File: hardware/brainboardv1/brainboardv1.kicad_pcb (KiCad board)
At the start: 4 copper layers, 86.4 x 54.6 mm, 86 parts, among them P1 WP, P2 CONN_12, P3 CONN_5X2, P4 BTRST, P5 GND, P6 5VD, P7 3V3, P8 5VA, U1 24C256, U10 TPS73150, U2 BEAGLEBONE_BLACK, U3 OPA2376, U4 ADS1299, U5 TPD4E001, U6 TPD4E001, U7 TPD4E001, U8 ATUC3L064, U9 BLUETOOTH-RN42

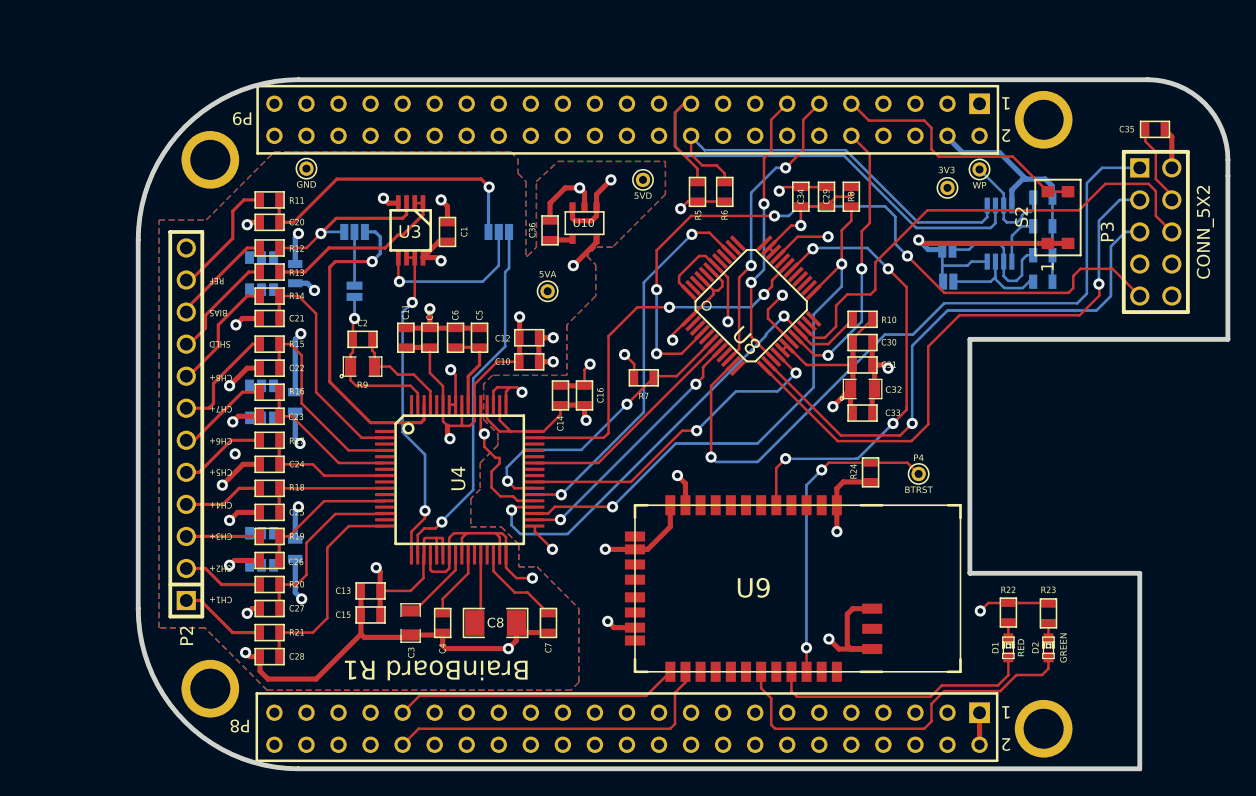
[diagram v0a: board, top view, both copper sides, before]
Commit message: Nearly finished v1 sch & brd, await final check
Fixed errors from Rev 0, added MPU-6050 accelerometer/gyro for head
motion tracking, switched to +/-2.5V analog supply, added 2 bipolar
analog inputs for EOG tracking, added daisy-chain capability
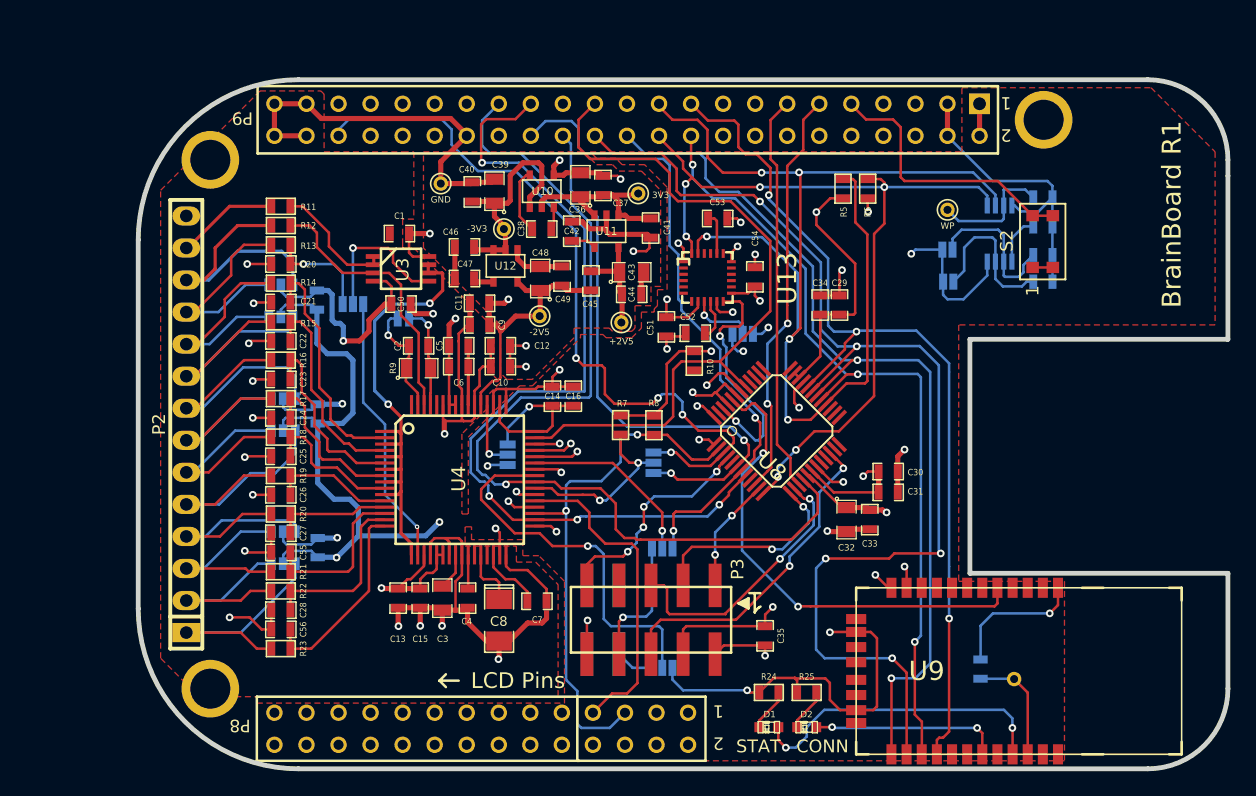
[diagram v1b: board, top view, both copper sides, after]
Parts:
- added C37: 1uF, SM0603_Capa, F.Cu at (189.2, 122.0)
- added C38: 1uF, SM0603_Capa, F.Cu at (184.4, 125.5)
- added C39: 10uF, SM0805, F.Cu at (180.6, 122.5)
- added C40: 1uF, SM0603_Capa, F.Cu at (178.9, 122.6)
- added C41: 1uF, SM0603_Capa, F.Cu at (193.0, 125.4)
- added C42: 0.01uF, SM0603_Capa, F.Cu at (186.8, 125.7)
- added C43: 10uF, SM0805, F.Cu at (191.5, 128.9)
- added C44: 2.2uF, SM0603_Capa, F.Cu at (191.5, 130.7)
- added C45: 0.1uF, SM0603_Capa, F.Cu at (188.3, 129.6)
- added C46: 1uF, SM0603_Capa, F.Cu at (178.3, 126.9)
- added C47: 0.01uF, SM0603_Capa, F.Cu at (178.3, 129.4)
- added C48: 10uF, SM0805, F.Cu at (184.3, 129.4)
- added C49: 2.2uF, SM0603_Capa, F.Cu at (186.0, 129.2)
- added C50: 0.1uF, SM0603_Capa, F.Cu at (173.2, 131.4)
- added C51: 0.1uF, SM0603_Capa, F.Cu at (194.3, 133.2)
- added C52: 0.1uF, SM0603_Capa, F.Cu at (196.5, 133.8)
- added C53: 2.2nF, SM0603_Capa, F.Cu at (198.3, 124.7)
- added C54: 0.01uF, SM0603_Capa, F.Cu at (201.3, 129.3)
- added C55: 4.7nF, SM0603_Capa, F.Cu at (163.7, 151.1)
- added C56: 4.7nF, SM0603_Capa, F.Cu at (163.7, 157.2)
- added P10: CONN_2X2, bb02-hp04, B.Cu at (189.2, 156.5)
- added P9: -2V5, PINTST, F.Cu at (184.2, 132.4)
- added R25: 330, SM0603, F.Cu at (205.4, 162.2)
- added R26: 10K, SM0603, B.Cu at (219.2, 160.4)
- added SJ6: DAISY_OUT, SparkFun-Passives-SJ_3_PASTE2&3, B.Cu at (193.9, 150.8)
- added SJ7: DAISY_CS, SparkFun-Passives-SJ_3_PASTE2&3, B.Cu at (193.9, 160.3)
- added SJ8: CLKSEL, SparkFun-Passives-SJ_3_PASTE1&2, B.Cu at (181.7, 143.4)
- added SJ9: I2C Address Select (2&3NC), SparkFun-Passives-SJ_3_PASTE2&3, B.Cu at (200.3, 133.8)
- added U11: TPS73225, SOT23-5, F.Cu at (189.5, 125.7)
- added U12: TPS72325, SOT23-5, F.Cu at (181.5, 128.4)
- added U13: MPU6050, QFN24-4x4, F.Cu at (197.5, 129.3)
- C1, C10, C11, C12, C13, C14, C15, C16, C17, C18, C19, C2, C20, C21, C22, C23, C24, C25, C26, C27, C28, C29, C30, C31, C33, C34, C35, C4, C5, C6, C7, C9: footprint SM0603 -> SM0603_Capa
- C36: value 0.1uF -> 10uF; footprint SM0603 -> SM0805
- C8: footprint SM1206 -> SM1206POL
- D1: value RED -> STAT
- D2: value GREEN -> CONN
- P2: value CONN_12 -> CONN_14; footprint PIN_ARRAY-12X1 -> pin_strip_14
- P3: footprint PIN_ARRAY_5x2 -> bb02-hp10
- P4: moved to B.Cu
- P6: value 5VD -> -3V3
- P8: value 5VA -> +2V5
- R22, R23: value 330 -> 4.99K
- R24: value 10K -> 330
- SJ1: value SOLDERJUMPER_2WAYPASTE2&3 -> REF-SRB2
- SJ2: value SOLDERJUMPER_2WAYPASTE2&3 -> DAISY_CS
- SJ3: value SOLDERJUMPERNO -> NO BIAS FILT
- SJ4: value SOLDERJUMPERNC2 -> A2
- SJ5: value SOLDERJUMPERNC2 -> A1
- U10: value TPS73150 -> TPS60403
- U2: footprint BEAGLEBONE_BLACK -> BEAGLEBONE_BLACK_EEGMOD
- U5, U6, U7: value TPD4E001 -> TPD4E001DBV
- moved R23 60.9 mm to (163.7, 158.8), turned to 0 degrees
- moved R22 57.7 mm to (163.7, 154.2), turned to 0 degrees
- moved C35 50.6 mm to (202.1, 157.7), turned to 270 degrees
- moved P3 50.4 mm to (193.0, 156.5), turned to 180 degrees
- moved SJ2 29.9 mm to (193.2, 144.0), turned to 270 degrees
- moved P7 24.5 mm to (192.0, 122.7)
- moved R8 23.9 mm to (193.3, 141.0)
- moved D2 20.2 mm to (205.4, 165.0), turned to 180 degrees
- moved D1 20.0 mm to (202.4, 165.0), turned to 180 degrees
- moved R24 19.2 mm to (202.4, 162.2), turned to 180 degrees
- moved U9 18.7 mm to (218.7, 160.5)
- moved P4 17.9 mm to (221.8, 161.2)
- moved R10 13.7 mm to (196.5, 135.9), turned to 270 degrees
- moved SJ1 12.9 mm to (169.4, 131.4)
- moved P6 11.7 mm to (181.4, 125.5)
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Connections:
- C1 pad 1: +5VA -> +2.5V
- C10 pad 1: +5VA -> +2.5V
- C11 pad 1: +5VA -> +2.5V
- C11 pad 2: AGND -> -2.5V
- C12 pad 1: +5VA -> +2.5V
- C13 pad 1: +5VA -> +2.5V
- C13 pad 2: AGND -> -2.5V
- C14 pad 1: 3V3 -> +3.3V
- C15 pad 1: +5VA -> +2.5V
- C15 pad 2: AGND -> -2.5V
- C16 pad 1: 3V3 -> +3.3V
- C17 pad 1: +5VA -> +2.5V
- C17 pad 2: AGND -> -2.5V
- C18 pad 1: +5VA -> +2.5V
- C18 pad 2: AGND -> -2.5V
- C19 pad 1: +5VA -> +2.5V
- C19 pad 2: AGND -> -2.5V
- C27 pad 1: AIN2P -> AIN2N
- C28 pad 1: AIN1P -> AIN1N
- C29 pad 1: 3V3 -> +3.3V
- C3 pad 1: AGND -> -2.5V
- C30 pad 1: 3V3 -> +3.3V
- C31 pad 1: 3V3 -> +3.3V
- C32 pad 1: 3V3 -> +3.3V
- C33 pad 1: 3V3 -> +3.3V
- C34 pad 1: 3V3 -> +3.3V
- C35 pad 1: 3V3 -> +3.3V
- C36 pad 1: N-00000204 -> +3.3V
- C4 pad 2: AGND -> -2.5V
- C5 pad 2: AGND -> -2.5V
- C6 pad 2: AGND -> -2.5V
- C7 pad 2: AGND -> -2.5V
- C8 pad 2: AGND -> -2.5V
- C9 pad 1: +5VA -> +2.5V
- C9 pad 2: AGND -> -2.5V
- D1 pad 2: N-00000194 -> N-00000159
- D2 pad 2: N-00000193 -> N-00000157
- P2 pad 10: /BrainBoard Analog In/BIAS_ELEC -> /BrainBoard Analog In/CH8ELEC_P
- P2 pad 12: (no net) -> /BrainBoard Analog In/BIAS_ELEC
- P2 pad 2: /BrainBoard Analog In/CH2ELEC_P -> /BrainBoard Analog In/CH1ELEC_N
- P2 pad 3: /BrainBoard Analog In/CH3ELEC_P -> /BrainBoard Analog In/CH2ELEC_P
- P2 pad 4: /BrainBoard Analog In/CH4ELEC_P -> /BrainBoard Analog In/CH2ELEC_N
- P2 pad 5: /BrainBoard Analog In/CH5ELEC_P -> /BrainBoard Analog In/CH3ELEC_P
- P2 pad 6: /BrainBoard Analog In/CH6ELEC_P -> /BrainBoard Analog In/CH4ELEC_P
- P2 pad 7: /BrainBoard Analog In/CH7ELEC_P -> /BrainBoard Analog In/CH5ELEC_P
- P2 pad 8: /BrainBoard Analog In/CH8ELEC_P -> /BrainBoard Analog In/CH6ELEC_P
- P2 pad 9: /BrainBoard Analog In/BIAS_SHD -> /BrainBoard Analog In/CH7ELEC_P
- P3 pad 4: 3V3 -> +3.3V
- P3 pad 8: (no net) -> DAISY_OUT
- P6 pad 1: +5VD -> -3.3V
- P7 pad 1: 3V3 -> +3.3V
- P8 pad 1: +5VA -> +2.5V
- R1 pad 1: 3V3 -> +3.3V
- R10 pad 1: 3V3 -> +3.3V
- R10 pad 2: /RESET -> /BrainBoard AFE//RESET
- R11 pad 1: /BrainBoard Analog In/REF_ELEC -> /BrainBoard Analog In/BIAS_SHD
- R11 pad 2: REF -> SHIELD
- R13 pad 1: /BrainBoard Analog In/BIAS_SHD -> /BrainBoard Analog In/REF_ELEC
- R13 pad 2: SHIELD -> REF
- R2 pad 1: 3V3 -> +3.3V
- R20 pad 1: /BrainBoard Analog In/CH2ELEC_P -> /BrainBoard Analog In/CH2ELEC_N
- R20 pad 2: AIN2P -> AIN2N
- R21 pad 1: /BrainBoard Analog In/CH1ELEC_P -> /BrainBoard Analog In/CH2ELEC_P
- R21 pad 2: AIN1P -> AIN2P
- R22 pad 1: N-00000194 -> /BrainBoard Analog In/CH1ELEC_N
- R22 pad 2: AGND -> AIN1N
- R23 pad 1: N-00000193 -> /BrainBoard Analog In/CH1ELEC_P
- R23 pad 2: AGND -> AIN1P
- R24 pad 1: /BrainBoard Bluetooth/FACTORY -> N-00000159
- R3 pad 1: 3V3 -> +3.3V
- R4 pad 1: 3V3 -> +3.3V
- R5 pad 1: 3V3 -> +3.3V
- R5 pad 2: /SCL -> I2C2_SCL
- R6 pad 1: 3V3 -> +3.3V
- R6 pad 2: /SDA -> I2C2_SDA
- R7 pad 1: 3V3 -> +3.3V
- R7 pad 2: /CS -> /BrainBoard AFE//CS
- R8 pad 1: 3V3 -> +3.3V
- SJ2 pad 1: /BrainBoard AFE/BIASIN -> /CS_DAISY
- SJ2 pad 2: N-0000099 -> /BrainBoard AFE//CS
- SJ2 pad 3: BIAS -> /CS_MAIN
- SJ3 pad 1: N-0000099 -> /BrainBoard AFE/BIASINV
- U1 pad 5: /SDA -> I2C2_SDA
- U1 pad 6: /SCL -> I2C2_SCL
- U1 pad 8: 3V3 -> +3.3V
- U10 pad 1: +5VD -> -3.3V
- U10 pad 2: AGND -> +3.3V
- U10 pad 3: +5VD -> N-00000168
- U10 pad 4: N-00000204 -> AGND
- U10 pad 5: +5VA -> N-00000167
- U2 pad A23: (no net) -> /PWDN
- U2 pad A25: (no net) -> CLK
- U2 pad A37: UARTBT_RX -> (no net)
- U2 pad A38: UARTBT_TX -> (no net)
- U2 pad B10: SYS_RESETn -> (no net)
- U2 pad B19: /SCL -> UARTBT_RTS
- U2 pad B20: /SDA -> UARTBT_CTS
- U2 pad B21: (no net) -> I2C2_SCL
- U2 pad B22: (no net) -> I2C2_SDA
- U2 pad B24: (no net) -> UARTBT_TX
- U2 pad B25: (no net) -> /DRDY
- U2 pad B26: (no net) -> UARTBT_RX
- U2 pad B28: (no net) -> /CS_MAIN
- U2 pad B29: (no net) -> MOSI
- U2 pad B3: 3V3 -> +3.3V
- U2 pad B30: (no net) -> MISO
- U2 pad B31: (no net) -> SCLK
- U2 pad B4: 3V3 -> +3.3V
- U2 pad B42: (no net) -> /CS_DAISY
- U2 pad B7: +5VD -> (no net)
- U2 pad B8: +5VD -> (no net)
- U3 pad 4: AGND -> -2.5V
- U3 pad 8: +5VA -> +2.5V
- U4 pad 1: (no net) -> /BrainBoard AFE/SRB1
- U4 pad 11: (no net) -> /BrainBoard AFE/SRB1
- U4 pad 13: (no net) -> AIN2N
- U4 pad 15: (no net) -> AIN1N
- U4 pad 19: +5VA -> +2.5V
- U4 pad 20: AGND -> -2.5V
- U4 pad 21: +5VA -> +2.5V
- U4 pad 22: +5VA -> +2.5V
- U4 pad 23: AGND -> -2.5V
- U4 pad 25: AGND -> -2.5V
- U4 pad 3: (no net) -> /BrainBoard AFE/SRB1
- U4 pad 32: AGND -> -2.5V
- U4 pad 36: /RESET -> +3.3V
- U4 pad 37: AGND -> CLK
- U4 pad 38: START -> AGND
- U4 pad 39: /CS -> /BrainBoard AFE//CS
- U4 pad 41: (no net) -> /BrainBoard AFE/DAISY
- U4 pad 42: (no net) -> AGND
- U4 pad 43: MISO -> /BrainBoard AFE/DOUT
- U4 pad 44: (no net) -> AGND
- U4 pad 45: (no net) -> AGND
- U4 pad 46: (no net) -> AGND
- U4 pad 48: 3V3 -> +3.3V
- U4 pad 5: (no net) -> /BrainBoard AFE/SRB1
- U4 pad 50: 3V3 -> +3.3V
- U4 pad 52: 3V3 -> /BrainBoard AFE/CLKSEL
- U4 pad 53: AGND -> -2.5V
- U4 pad 54: +5VA -> +2.5V
- U4 pad 56: +5VA -> +2.5V
- U4 pad 57: AGND -> -2.5V
- U4 pad 58: AGND -> -2.5V
- U4 pad 59: +5VA -> +2.5V
- U4 pad 62: /BrainBoard AFE/BIASIN -> BIAS
- U4 pad 7: (no net) -> /BrainBoard AFE/SRB1
- U4 pad 9: (no net) -> /BrainBoard AFE/SRB1
- U5 pad 1: /BrainBoard Analog In/CH3ELEC_P -> /BrainBoard Analog In/CH2ELEC_P
- U5 pad 2: /BrainBoard Analog In/CH4ELEC_P -> -2.5V
- U5 pad 3: AGND -> /BrainBoard Analog In/CH2ELEC_N
- U5 pad 5: /BrainBoard Analog In/CH2ELEC_P -> +2.5V
- U5 pad 6: +5VA -> /BrainBoard Analog In/CH1ELEC_N
- U6 pad 1: /BrainBoard Analog In/CH7ELEC_P -> /BrainBoard Analog In/CH5ELEC_P
- U6 pad 2: /BrainBoard Analog In/CH8ELEC_P -> -2.5V
- U6 pad 3: AGND -> /BrainBoard Analog In/CH6ELEC_P
- U6 pad 4: /BrainBoard Analog In/CH5ELEC_P -> /BrainBoard Analog In/CH3ELEC_P
- U6 pad 5: /BrainBoard Analog In/CH6ELEC_P -> +2.5V
- U6 pad 6: +5VA -> /BrainBoard Analog In/CH4ELEC_P
- U7 pad 2: /BrainBoard Analog In/BIAS_ELEC -> -2.5V
- U7 pad 3: AGND -> /BrainBoard Analog In/BIAS_ELEC
- U7 pad 4: /BrainBoard Analog In/BIAS_SHD -> /BrainBoard Analog In/CH7ELEC_P
- U7 pad 5: (no net) -> +2.5V
- U7 pad 6: +5VA -> /BrainBoard Analog In/CH8ELEC_P
- U8 pad 12: (no net) -> I2C2_SDA
- U8 pad 17: 3V3 -> +3.3V
- U8 pad 18: 3V3 -> +3.3V
- U8 pad 2: (no net) -> /PWDN
- U8 pad 20: SYS_RESETn -> (no net)
- U8 pad 21: /RESET -> (no net)
- U8 pad 25: /PWDN -> (no net)
- U8 pad 28: (no net) -> I2C2_SCL
- U8 pad 29: (no net) -> UARTBT_CTS
- U8 pad 3: (no net) -> /CS_DAISY
- U8 pad 30: RESET_BT -> UARTBT_TX
- U8 pad 31: /DRDY -> UARTBT_RX
- U8 pad 32: (no net) -> UARTBT_RTS
- U8 pad 34: 3V3 -> +3.3V
- U8 pad 35: 3V3 -> +3.3V
- U8 pad 39: START -> (no net)
- U8 pad 41: (no net) -> /DRDY
- U8 pad 42: 3V3 -> +3.3V
- U8 pad 44: (no net) -> RESET_BT
- U8 pad 46: (no net) -> IMU_INT
- U8 pad 48: 3V3 -> +3.3V
- U8 pad 6: /CS -> /CS_MAIN
- U9 pad 11: 3V3 -> +3.3V
- U9 pad 13: UARTBT_RX -> UARTBT_TX
- U9 pad 14: UARTBT_TX -> UARTBT_RX
- U9 pad 15: (no net) -> UARTBT_CTS
- U9 pad 16: (no net) -> UARTBT_RTS
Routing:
- net +3.3V: track 0.00 -> 226.6 mm, vias 0 -> 14
- net -2.5V: track 0.00 -> 168.1 mm, vias 0 -> 9
- net 3V3: track 159.8 -> 0.00 mm, vias 7 -> 0
- net +2.5V: track 0.00 -> 139.0 mm, vias 0 -> 5
- net +5VA: track 117.2 -> 0.00 mm, vias 8 -> 0
- net I2C2_SCL: track 0.00 -> 92.9 mm, vias 0 -> 5
- net UARTBT_RTS: track 0.00 -> 72.3 mm, vias 0 -> 3
- net UARTBT_RX: track 22.6 -> 90.1 mm, vias 0 -> 5
- net I2C2_SDA: track 0.00 -> 66.9 mm, vias 0 -> 6
- net UARTBT_CTS: track 0.00 -> 65.1 mm, vias 0 -> 3
- net /CS_DAISY: track 0.00 -> 59.6 mm, vias 0 -> 4
- net SCLK: track 26.3 -> 76.1 mm, vias 2 -> 1
- net MOSI: track 20.7 -> 69.5 mm, vias 2 -> 4
- net /BrainBoard MCU/TCK: track 57.1 -> 9.10 mm, vias 1 -> 2
- net UARTBT_TX: track 26.7 -> 72.7 mm, vias 0 -> 2
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- added copper zone on Power, net +3.3V
- removed copper zone on Power, net +5VA
- removed copper zone on Power, net +5VD
- removed copper zone on Power, net 3V3
- removed copper zone on B.Cu, net AGND
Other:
- outline, holes or cut-outs redrawn
- net class Critical Analog: via_dia 0.889 -> 0.6096; via_drill 0.635 -> 0.3048
- net class Default: via_dia 0.889 -> 0.6096; via_drill 0.635 -> 0.3048
- net class Power: via_dia 0.889 -> 0.6096; via_drill 0.635 -> 0.3048
- rule via_min_drill: 0.3302 -> 0.254
- rule via_min_size: 0.508 -> 0.3556
- board text added: "LCD Pins"
- board text removed: "BIAS"
- board text removed: "CH1+"
- board text removed: "CH2+"
- board text removed: "CH3+"
- board text removed: "CH4+"
- board text removed: "CH5+"
- board text removed: "CH6+"
- board text removed: "CH7+"
- board text removed: "CH8+"
- board text removed: "REF"
- board text removed: "SHLD"

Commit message: Added thicker power traces and fixed silkscreen
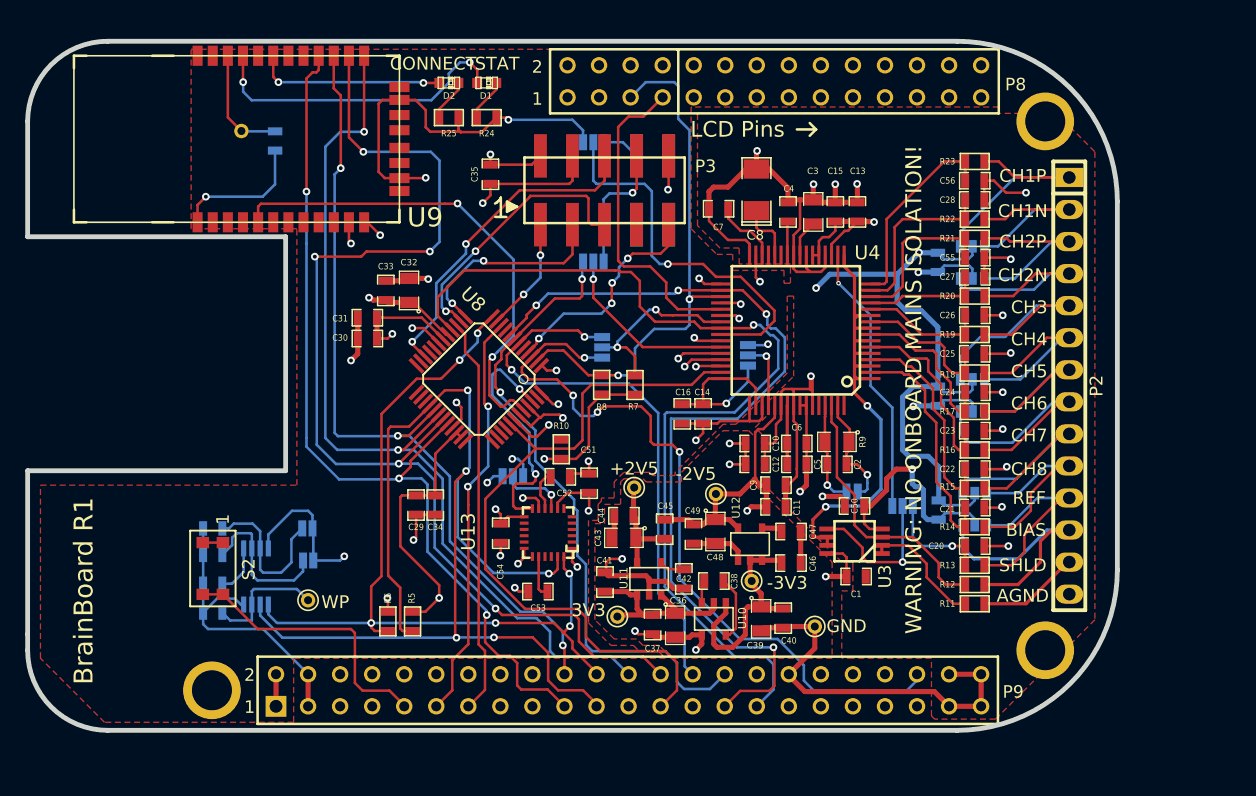
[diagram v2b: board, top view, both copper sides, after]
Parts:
- D2: value CONN -> CONNECT
- moved P4 75.1 mm to (160.6, 117.7), turned to 180 degrees
- moved R4 73.6 mm to (158.3, 155.9), turned to 0 degrees
- moved R3 71.6 mm to (158.3, 153.6), turned to 0 degrees
- moved S2 71.1 mm to (158.1, 152.4), turned to 90 degrees
- moved P2 70.0 mm to (226.2, 137.9), turned to 270 degrees
- moved R2 69.9 mm to (158.3, 151.3), turned to 0 degrees
- moved R26 69.8 mm to (163.2, 118.5), turned to 270 degrees
- moved U9 69.3 mm to (163.7, 118.4), turned to 0 degrees
- moved R1 68.6 mm to (158.3, 149.2), turned to 0 degrees
- moved R23 67.2 mm to (218.7, 120.1), turned to 180 degrees
- moved C56 65.5 mm to (218.7, 121.7), turned to 0 degrees
- moved U1 64.9 mm to (161.7, 153.0), turned to 0 degrees
- moved C28 63.9 mm to (218.7, 123.2), turned to 0 degrees
- moved R11 63.4 mm to (218.7, 155.2), turned to 180 degrees
- moved R22 62.4 mm to (218.7, 124.7), turned to 180 degrees
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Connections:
- P2 pad 14: (no net) -> AGND
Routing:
- net +3.3V: track 226.6 -> 225.9 mm
- added copper zone on Power, net +2.5V
- added copper zone on Power, net -2.5V
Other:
- outline, holes or cut-outs redrawn
- board text added: "0"
- board text added: "AGND"
- board text added: "BIAS"
- board text added: "CH1N"
- board text added: "CH1P"
- board text added: "CH2N"
- board text added: "CH2P"
- board text added: "CH3"
- board text added: "CH4"
- board text added: "CH5"
- board text added: "CH6"
- board text added: "CH7"
- board text added: "CH8"
- board text added: "DAISY"
- board text added: "DAISY_IN"
- board text added: "GND"
- board text added: "MAIN"
- board text added: "MISO"
- board text added: "REF"
- board text added: "SHLD"
- board text added: "WARNING: NO ONBOARD MAINS ISOLATION!"

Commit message: Added bottom layer ground plane
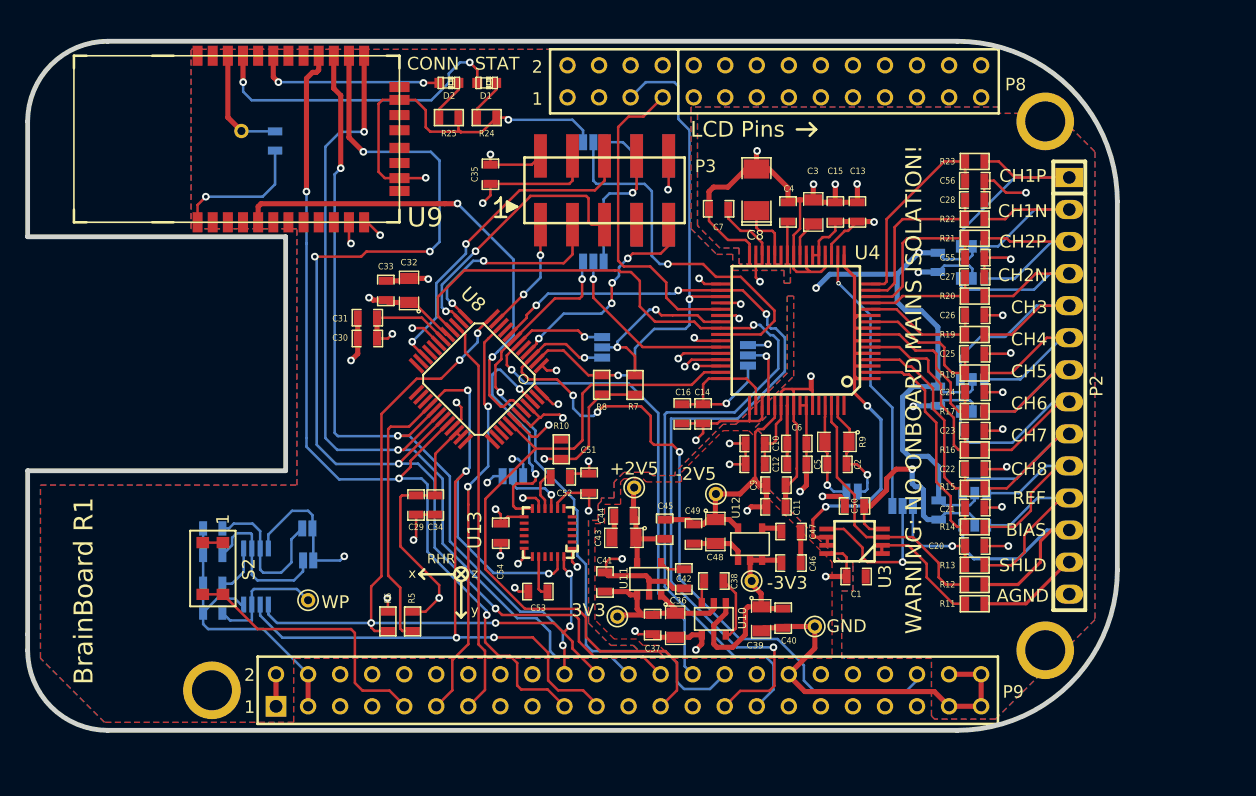
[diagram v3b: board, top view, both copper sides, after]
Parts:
- D2: value CONNECT -> CONN
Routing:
- added copper zone on B.Cu, net AGND
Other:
- rule pad_to_mask_clearance: 0.1524 -> 0.0254
- board text added: "RHR"
- board text added: "x"
- board text added: "y"
- board text added: "z"
